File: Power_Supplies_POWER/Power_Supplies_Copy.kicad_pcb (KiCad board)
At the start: 4 copper layers, 65.2 x 45 mm, 53 parts, among them IC1 NCP731ADNADJR2G, IC2 LT8338, IC6 TLV71209DBVT, IC7 TPS73618DBVTG4, IC8 TLV73333PDBVR, IC9 TLV73333PDBVR, J1 PINHD_1x4_Female, J23 PINHD_1x2_Female, J24 PINHD_1x2_Female, J25 Screw_Terminal_4_P5.00mm, J26 PINHD_1x1_Female, J28 PINHD_1x5_Female, J29 PINHD_1x2_Female, J30 PINHD_1x2_Female, J31 PINHD_1x2_Female, J32 PINHD_1x1_Female

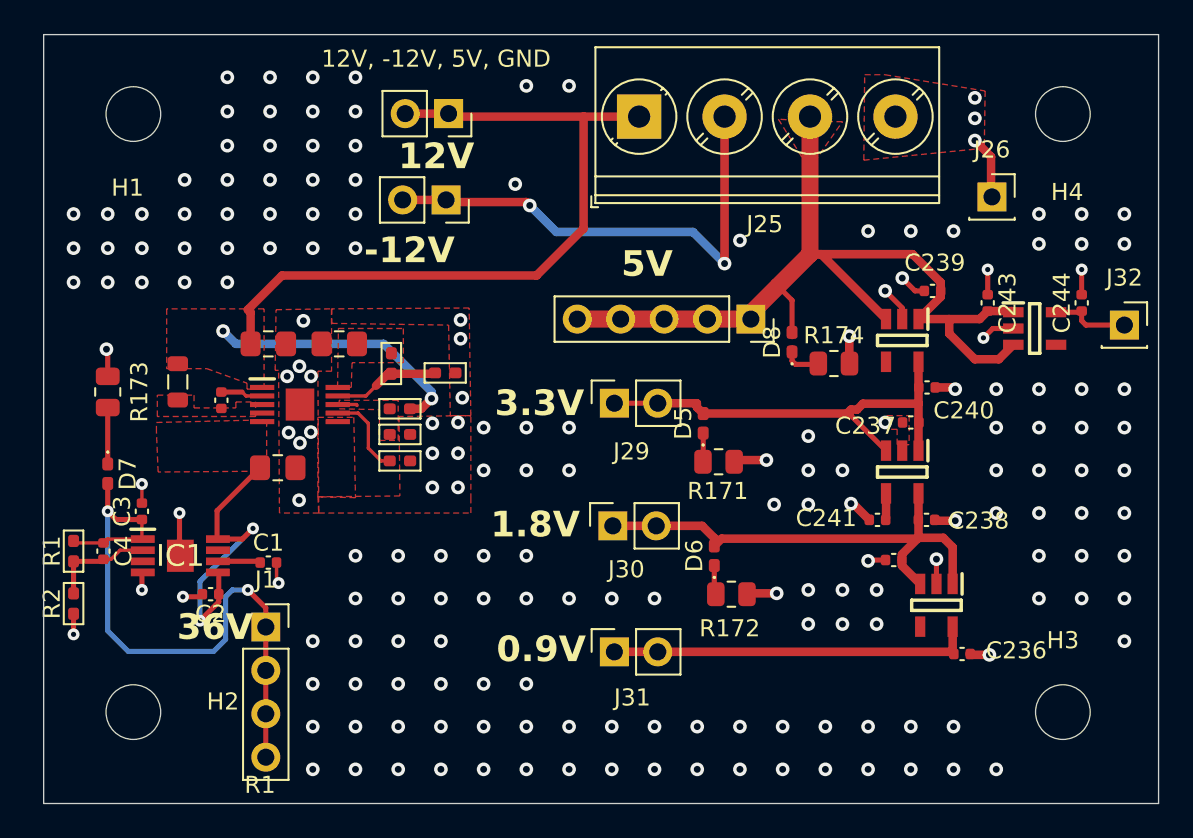
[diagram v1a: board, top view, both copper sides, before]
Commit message: fixed power board problems/...
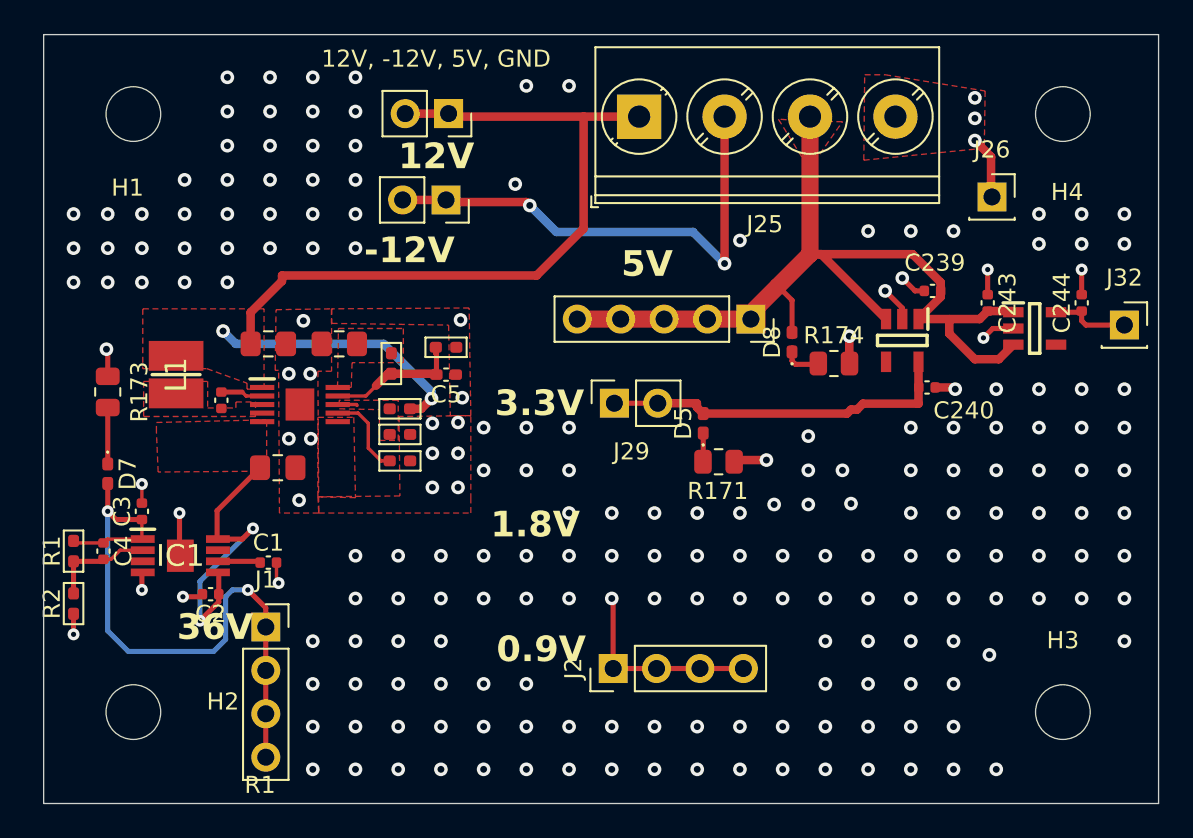
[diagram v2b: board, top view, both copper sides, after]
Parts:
- removed C233, C236, C237, C238: 1uF, Capacitor_SMD:C_0402_1005Metric
- removed C241: 0.1uF, Capacitor_SMD:C_0402_1005Metric
- removed D6: LED, LED_SMD:LED_0402_1005Metric_Pad0.77x0.64mm_HandSolder
- removed IC6: TLV71209DBVT, SamacSys_Parts:SOT95P280X145-5N
- removed IC7: TPS73618DBVTG4, SamacSys_Parts:SOT95P280X145-5N
- removed J30, J31: PINHD_1x2_Female, Connector_PinSocket_2.54mm:PinSocket_1x02_P2.54mm_Vertical
- removed L4: 10uH, Inductor_SMD:L_0805_2012Metric
- removed R172: 2.2k, Resistor_SMD:R_0805_2012Metric
- added C5: 0.01uF, Capacitor_SMD:C_0402_1005Metric_Pad0.74x0.62mm_HandSolder, F.Cu at (147.8, 59.4)
- added J2: PINHD_1x4_Male, Connector_PinHeader_2.54mm:PinHeader_1x04_P2.54mm_Vertical, F.Cu at (157.6, 76.6)
- added L1: 78438336100, SamacSys_Parts:INDC3030X200N, F.Cu at (132.0, 59.4)
- C52: value 2.2uF -> 0.1uF
- moved R41 1.50 mm to (147.8, 57.8)
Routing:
- net 1.8V: track 29.4 -> 0.00 mm
- net 0.9V: track 21.5 -> 0.00 mm
- net 3.3V: track 27.5 -> 21.5 mm
- net GND: track 34.9 -> 38.6 mm, vias 189 -> 213
- net Net-(D6-Pad1): track 1.71 -> 0.00 mm
- net Net-(IC2-CTRL): track 6.25 -> 7.80 mm
- net Net-(IC7-NR/FB): track 1.48 -> 0.00 mm

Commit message: made new pcbs :(
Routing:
- net GND: vias 213 -> 215
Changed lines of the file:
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@@
 		)
 		(fp_text user "${REFERENCE}"
-			(at 0 3.81 360)
+			(at 0 3.81 0)
 			(layer "F.Fab")
 			(effects
@@
 	)
 	(segment
-		(start 138.2 53.6)
-		(end 138.2 53.925)
+		(start 155.85 44.3)
+		(end 155.85 50.85)
 		(width 0.5)
 		(layer "F.Cu")
@@
 	)
 	(segment
-		(start 155.85 50.85)
-		(end 153.1 53.6)
+		(start 137.8 53.6)
+		(end 136.3625 55.0375)
 		(width 0.5)
 		(layer "F.Cu")
@@
 	)
 	(segment
-		(start 153.1 53.6)
-		(end 138.2 53.6)
+		(start 155.85 44.3)
+		(end 148.125 44.3)
 		(width 0.5)
 		(layer "F.Cu")
@@
 	)
 	(segment
-		(start 155.85 44.3)
-		(end 148.125 44.3)
+		(start 153.1 53.6)
+		(end 137.8 53.6)
 		(width 0.5)
 		(layer "F.Cu")
@@
 	)
 	(segment
-		(start 136.3625 55.7625)
-		(end 136.3625 57.6)
+		(start 155.85 50.85)
+		(end 153.1 53.6)
 		(width 0.5)
 		(layer "F.Cu")
@@
 	)
 	(segment
-		(start 138.2 53.925)
-		(end 136.3625 55.7625)
-		(width 0.5)
-		(layer "F.Cu")
-		(net 2)
-	)
-	(segment
 		(start 147.95 44.125)
 		(end 145.41 44.125)
@@
 	)
 	(segment
-		(start 155.85 44.3)
-		(end 155.85 50.85)
+		(start 136.3625 55.0375)
+		(end 136.3625 57.6)
 		(width 0.5)
 		(layer "F.Cu")
@@
 	)
 	(via
+		(at 143.7 67)
+		(size 0.8)
+		(drill 0.4)
+		(layers "F.Cu" "B.Cu")
+		(free yes)
+		(net 4)
+	)
+	(via
 		(at 177.5 80)
 		(size 0.8)
@@
 	)
 	(via
-		(at 147 66)
-		(size 0.8)
-		(drill 0.4)
-		(layers "F.Cu" "B.Cu")
-		(free yes)
-		(net 4)
-	)
-	(via
 		(at 147.5 75)
 		(size 0.8)
@@
 	)
 	(via
-		(at 147 64)
-		(size 0.8)
-		(drill 0.4)
-		(layers "F.Cu" "B.Cu")
-		(free yes)
-		(net 4)
-	)
-	(via
 		(at 180 72.5)
 		(size 0.8)
@@
 	)
 	(via
-		(at 148.5 64)
-		(size 0.8)
-		(drill 0.4)
-		(layers "F.Cu" "B.Cu")
-		(free yes)
-		(net 4)
-	)
-	(via
 		(at 172.5 80)
 		(size 0.8)
@@
 	)
 	(via
-		(at 148.5 66)
-		(size 0.8)
-		(drill 0.4)
-		(layers "F.Cu" "B.Cu")
-		(free yes)
-		(net 4)
-	)
-	(via
 		(at 187.5 72.5)
 		(size 0.8)
@@
 	)
 	(via
+		(at 145.6 67)
+		(size 0.8)
+		(drill 0.4)
+		(layers "F.Cu" "B.Cu")
+		(free yes)
+		(net 4)
+	)
+	(via
 		(at 157.5 80)
 		(size 0.8)
@@
 	)
 	(via
+		(at 147.3 56.05)
+		(size 0.7)
+		(drill 0.3)
+		(layers "F.Cu" "B.Cu")
+		(free yes)
+		(net 4)
+	)
+	(via
 		(at 177.6 60.25)
 		(size 0.8)
@@
 	)
 	(via
+		(at 141.4 65.85)
+		(size 0.8)
+		(drill 0.4)
+		(layers "F.Cu" "B.Cu")
+		(free yes)
+		(net 4)
+	)
+	(via
 		(at 127.925 57.9125)
 		(size 0.8)
@@
 	)
 	(via
+		(at 141.4 64.35)
+		(size 0.8)
+		(drill 0.4)
+		(layers "F.Cu" "B.Cu")
+		(free yes)
+		(net 4)
+	)
+	(via
 		(at 171.4 57.15)
 		(size 0.8)
@@
 	)
 	(via
+		(at 147.6 65.1)
+		(size 0.8)
+		(drill 0.4)
+		(layers "F.Cu" "B.Cu")
+		(free yes)
+		(net 4)
+	)
+	(via
 		(at 182.5 62.5)
 		(size 0.8)
@@
 	)
 	(segment
-		(start 134.5 71.025)
-		(end 134.45 70.975)
-		(width 0.2)
+		(start 134.45 69.025)
+		(end 134.45 67.3125)
+		(width 0.3)
 		(layer "F.Cu")
 		(net 13)
 	)
 	(segment
-		(start 134.4 67.3625)
-		(end 134.4 68.975)
-		(width 0.3)
+		(start 134.5 71.025)
+		(end 134.45 70.975)
+		(width 0.2)
 		(layer "F.Cu")
 		(net 13)
 	)
 	(segment
-		(start 136.9125 64.85)
-		(end 134.4 67.3625)
+		(start 134.45 67.3125)
+		(end 136.9125 64.85)
 		(width 0.3)
 		(layer "F.Cu")
@@
 	(segment
 		(start 147.2025 57.8)
-		(end 147.2025 58.1625)
-		(width 0.3)
+		(end 147.2025 59.25)
+		(width 0.5)
 		(layer "F.Cu")
 		(net 15)
@@
 	)
 	(segment
-		(start 144.6 59.3475)
-		(end 147.105 59.3475)
+		(start 147.2025 59.25)
+		(end 147.1525 59.3)
 		(width 0.5)
 		(layer "F.Cu")
@@
 	)
 	(segment
-		(start 147.2025 58.1625)
-		(end 147.24 58.2)
-		(width 0.3)
-		(layer "F.Cu")
-		(net 15)
-	)
-	(segment
-		(start 147.24 58.2)
-		(end 147.24 59.2125)
-		(width 0.3)
+		(start 144.6 59.3475)
+		(end 147.105 59.3475)
+		(width 0.5)
 		(layer "F.Cu")
 		(net 15)
@@
 	)
 	(segment
-		(start 144.5025 64.45)
-		(end 144 64.45)
-		(width 0.2)
+		(start 143.25 63.1975)
+		(end 143.25 62.25)
+		(width 0.5)
 		(layer "F.Cu")
 		(net 16)
 	)
 	(segment
-		(start 144 64.45)
-		(end 143.25 63.7)
-		(width 0.2)
+		(start 144.5025 64.45)
+		(end 143.25 63.1975)
+		(width 0.5)
 		(layer "F.Cu")
 		(net 16)
@@
 	)
 	(segment
-		(start 143.25 63.7)
-		(end 143.25 62.25)
-		(width 0.2)
-		(layer "F.Cu")
-		(net 16)
-	)
-	(segment
 		(start 185 56.25)
 		(end 185.25 56.5)
@@
 		(polygon
 			(pts
-				(xy 141.45 60.15) (xy 141.5 56.7) (xy 145.3 56.7) (xy 145.3 58.7) (xy 142.3 58.7) (xy 142.25 60.15)
+				(xy 141.65 60.15) (xy 141.7 56.6) (xy 145.3 56.7) (xy 145.3 58.7) (xy 142.3 58.7) (xy 142.25 60.25)
 			)
 		)
@@
 		(polygon
 			(pts
-				(xy 136.65 61.85) (xy 130.1 61.85) (xy 130.1 59.8) (xy 133.85 59.8) (xy 133.85 61.35) (xy 135.5 61.35)
+				(xy 136.65 61.85) (xy 130.1 61.85) (xy 130.1 59.8) (xy 133.85 59.8) (xy 133.85 61.2) (xy 135.5 61.2)
 				(xy 135.5 61) (xy 136.65 61)
 			)
@@
 		(polygon
 			(pts
-				(xy 149.25 61.8) (xy 149.15 55.5) (xy 141.1 55.55) (xy 141.1 56.4) (xy 147.95 56.5) (xy 148.05 61.8)
+				(xy 149.25 61.8) (xy 149.15 55.5) (xy 141.1 55.55) (xy 141.1 56.4) (xy 147.95 56.5) (xy 147.95 61.8)
 			)
 		)

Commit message: aaaah (cooked)
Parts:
- removed C242: 4.7uF, Capacitor_SMD:C_0805_2012Metric_Pad1.18x1.45mm_HandSolder
- removed C5: 0.01uF, Capacitor_SMD:C_0402_1005Metric_Pad0.74x0.62mm_HandSolder
- removed C51, C53: 2.2uF, Capacitor_SMD:C_0805_2012Metric_Pad1.18x1.45mm_HandSolder
- removed C52: 0.1uF, Capacitor_SMD:C_0402_1005Metric
- removed IC2: LT8338, SamacSys_Parts:SOP50P490X110-11N
- removed L1: 78438336100, SamacSys_Parts:INDC3030X200N
- removed R37, R41: 1M, PCM_Resistor_SMD_AKL:R_0402_1005Metric_Pad0.72x0.64mm_HandSolder
- removed R38: 162k, PCM_Resistor_SMD_AKL:R_0402_1005Metric_Pad0.72x0.64mm_HandSolder
- removed R39: 40.2k, PCM_Resistor_SMD_AKL:R_0402_1005Metric_Pad0.72x0.64mm_HandSolder
- removed R40: 301k, PCM_Resistor_SMD_AKL:R_0402_1005Metric_Pad0.72x0.64mm_HandSolder
- added C6: 1.5nF, Capacitor_SMD:C_0805_2012Metric_Pad1.18x1.45mm_HandSolder, F.Cu at (148.8, 65.9)
- added C7: 100uF_50V, Capacitor_SMD:CP_Elec_6.3x5.4, F.Cu at (149.9, 51.0)
- added C8: 330uF_35V, Capacitor_SMD:CP_Elec_10x10.5, F.Cu at (147.1, 77.4)
- added D1: TMBYV10-40FILM, SamacSys_Parts:TMBYV1040FILM, F.Cu at (142.3, 67.8)
- added IC3: MC34063ECD-TR, SamacSys_Parts:SOIC127P600X175-8N, F.Cu at (146.9, 60.2)
- added L2: 180uH, Inductor_SMD:L_Vishay_IHLP-1212, F.Cu at (142.1, 60.6)
- added R3: 180, PCM_Resistor_SMD_AKL:R_0805_2012Metric_Pad1.15x1.40mm_HandSolder, F.Cu at (142.1, 53.1)
- added R4: 0.22, PCM_Resistor_SMD_AKL:R_2512_6332Metric_Pad1.40x3.35mm_HandSolder, F.Cu at (140.0, 48.9)
- added R5: 10k, PCM_Resistor_SMD_AKL:R_0805_2012Metric_Pad1.15x1.40mm_HandSolder, F.Cu at (151.1, 61.1)
- added R6: 280k, PCM_Resistor_SMD_AKL:R_0805_2012Metric_Pad1.15x1.40mm_HandSolder, F.Cu at (153.9, 61.1)
- J26, J32: value PINHD_1x1_Female -> PINHD_1x2_Female; footprint Connector_PinSocket_2.54mm:PinSocket_1x01_P2.54mm_Vertical -> Connector_PinSocket_2.54mm:PinSocket_1x02_P2.54mm_Vertical
- moved J24 13.3 mm to (160.8, 52.2)
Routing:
- net 36V: track 17.8 -> 48.3 mm
- net Net-(IC3-IPK): track 0.00 -> 19.5 mm
- net 12V: track 59.7 -> 40.2 mm, vias 2 -> 0
- net GND: track 38.6 -> 55.9 mm, vias 215 -> 176
- net -12V: track 29.0 -> 13.6 mm, vias 2 -> 0
- net Net-(IC3-SWC): track 0.00 -> 8.38 mm
- net Net-(IC2-CTRL): track 7.89 -> 0.00 mm
- net Net-(IC3-CII): track 0.00 -> 7.51 mm
- net Net-(IC3-DRC): track 0.00 -> 5.97 mm
- net Net-(IC2-RT): track 4.76 -> 0.00 mm
- net Net-(IC3-TC): track 0.00 -> 3.07 mm
- net 3.3V_2: track 4.70 -> 7.24 mm
- net BST: track 2.48 -> 0.00 mm
- net EN/UVLO: track 1.16 -> 0.00 mm
- removed copper zone on F.Cu, net 12V
- removed copper zone on F.Cu, net 36V
- removed copper zone on F.Cu, net EN/UVLO
- removed copper zone on F.Cu, net Net-(IC2-INTVCC)
- removed copper zone on F.Cu, net SW
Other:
- board text added: "Booster"
- board text added: "GND"
- board text removed: "0.9V"
- board text removed: "1.8V"
